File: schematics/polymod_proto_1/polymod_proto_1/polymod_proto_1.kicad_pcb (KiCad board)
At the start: 2 copper layers, 141 parts, among them J1 AudioJack2, J1 Conn_01x02_Male, J10 Conn_01x08_Male, J11 Conn_01x08_Male, J12 Conn_01x08_Male, J13 Conn_01x08_Male, J14 Conn_01x03_Male, J2 AudioJack3, J2 Conn_01x03_Male, J3 AudioJack2, J3 Conn_01x02_Male, J4 Barrel_Jack, J5 AudioJack3, J6 Conn_01x08_Male, J7 Conn_01x08_Male, J8 Conn_01x08_Male, J9 Conn_01x08_Male, SW1 SW_Push, SW2 SW_Push, SW3 SW_Push, SW4 SW_Push, SW5 SW_Push, SW6 SW_Push, SW7 SW_Push, SW8 SW_Push, U1 6N138, U10 74HC595, U11 74LS165, U12 74LS165, U13 74LS165, U2 74HC595, U3 74LS165, U4 4051, U5 74HC595, U6 74LS165, U7 4051, U8 74HC595, U9 74HC595

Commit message: layout going well
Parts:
- D10, D11, D12, D13, D14, D15, D16, D17, D18, D19, D20, D21, D22, D23, D24, D25, D26, D27, D28, D29, D30, D31, D32, D33, D34, D35, D36, D37, D38, D7, D8, D9: footprint Diode_THT:D_DO-35_SOD27_P7.62mm_Horizontal -> Diode_SMD:Nexperia_CFP3_SOD-123W
- moved C1 181.0 mm to (40.1, -81.9)
- moved D5 181.0 mm to (86.9, -120.7)
- moved D6 181.0 mm to (60.9, -92.2)
- moved J1 181.0 mm to (71.3, -105.7)
- moved JP1 181.0 mm to (75.9, -105.7)
- moved R1 181.0 mm to (55.0, -85.9)
- moved R10 181.0 mm to (94.2, -123.0)
- moved R5 181.0 mm to (98.6, -123.0)
- moved SW1 181.0 mm to (68.0, -122.5)
- moved SW5 181.0 mm to (49.9, -93.9)
- moved U2 181.0 mm to (53.3, -118.8)
- moved U3 181.0 mm to (61.7, -118.8)
- moved U4 181.0 mm to (160.1, -118.8)
- moved D1 181.0 mm to (47.7, -76.3)
- moved D2 181.0 mm to (47.8, -82.0)
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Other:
- board text added: "TEST LABEL TEST LABEL TEST LABEL TEST LABEL TEST LABEL TEST LABEL TEST LABEL TEST LABEL"

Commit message: components pretty much in place
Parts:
- removed the J1 at (71.3, -105.7)
- removed the J2 at (44.3, -93.2)
- removed the J3 at (71.3, -98.5)
- removed J5: AudioJack3, Connector_PinHeader_2.54mm:PinHeader_1x03_P2.54mm_Vertical
- SW1, SW2, SW3, SW4, SW5, SW6, SW7, SW8: footprint Button_Switch_THT:SW_PUSH_6mm_H4.3mm -> Button_Switch_THT:SW_PUSH-12mm
- moved SW6 335.5 mm to (215.9, 189.1), turned to 90 degrees
- moved SW7 333.5 mm to (188.0, 188.0), turned to 90 degrees
- moved SW8 331.9 mm to (200.7, 188.0), turned to 90 degrees
- moved J3 295.2 mm to (130.8, 132.1)
- moved J1 292.7 mm to (127.0, 132.1)
- moved SW5 282.8 mm to (198.1, 146.9), turned to 90 degrees
- moved SW1 278.3 mm to (137.2, 147.1), turned to 90 degrees
- moved SW2 277.3 mm to (152.4, 147.1), turned to 90 degrees
- moved SW3 271.5 mm to (167.7, 146.9), turned to 90 degrees
- moved SW4 270.3 mm to (182.9, 146.9), turned to 90 degrees
- moved D5 267.2 mm to (116.8, 144.8)
- moved R10 264.4 mm to (124.5, 139.7)
- moved D3 258.5 mm to (101.6, 144.8)
- moved U3 255.8 mm to (118.1, 130.8)
- moved U2 246.9 mm to (87.6, 125.7)
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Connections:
- J2 pad 2: /midi_in_ring -> /midi_out_ring
- J2 pad 3: /midi_in_tip -> /midi_out_tip
- R4 pad 2: /midi_in_ring -> /midi_out_ring
- R5 pad 1: /midi_in_tip -> /midi_out_tip

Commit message: routing started
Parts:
- removed SW6, SW7, SW8: SW_Push, Button_Switch_THT:SW_PUSH-12mm
- A1: moved to B.Cu
- moved U2 44.4 mm to (132.0, 124.0)
- moved U3 30.2 mm to (147.0, 122.0)
- moved J1 25.6 mm to (132.2, 107.0)
- moved J3 25.6 mm to (136.0, 107.0)
- moved A1 21.8 mm to (141.6, 62.5), turned to 180 degrees
- moved U4 20.8 mm to (148.0, 91.0)
- moved U7 20.2 mm to (148.0, 103.0)
- moved U10 8.71 mm to (88.0, 123.0), turned to 0 degrees
- moved U13 6.71 mm to (117.0, 126.0)
- moved R10 6.69 mm to (125.9, 146.2)
- moved R7 6.69 mm to (103.1, 146.2)
- moved R8 6.69 mm to (110.7, 146.2)
- moved R6 6.69 mm to (95.5, 146.2)
- moved R9 6.69 mm to (118.3, 146.2)
- moved R11 5.08 mm to (105.4, 55.9), turned to 180 degrees
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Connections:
- U3 pad 4: Net-(SW6-Pad2) -> unconnected-(U3-Pad4)
- U3 pad 5: Net-(SW7-Pad2) -> unconnected-(U3-Pad5)
- U3 pad 6: Net-(SW8-Pad2) -> unconnected-(U3-Pad6)
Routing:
- net Net-(SW5-Pad2): track 0.00 -> 77.5 mm
- net Net-(SW4-Pad2): track 0.00 -> 56.8 mm
- net Net-(R6-Pad1): track 0.00 -> 48.7 mm
- net Net-(R7-Pad1): track 0.00 -> 44.1 mm
- net Net-(SW3-Pad2): track 0.00 -> 41.5 mm
- net Net-(R8-Pad1): track 0.00 -> 39.3 mm
- net Net-(R9-Pad1): track 0.00 -> 32.7 mm
- net Net-(R10-Pad1): track 0.00 -> 30.4 mm
- net Net-(J7-Pad8): track 0.00 -> 29.5 mm
- net Net-(J12-Pad8): track 0.00 -> 29.4 mm
- net Net-(SW1-Pad2): track 0.00 -> 28.9 mm
- net Net-(J11-Pad8): track 0.00 -> 28.6 mm
- net Net-(J13-Pad8): track 0.00 -> 28.0 mm
- net Net-(SW2-Pad2): track 0.00 -> 28.0 mm
- net Net-(J7-Pad7): track 0.00 -> 27.8 mm
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- added copper zone on F.Cu, net GND

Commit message: routing is HARD
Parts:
- moved J14 63.5 mm to (172.5, 58.0), turned to 90 degrees
- moved D1 5.37 mm to (102.0, 38.0)
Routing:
- net VCC: track 0.00 -> 487.9 mm, vias 0 -> 4
- net PATCHING_OUT_LATCH: track 0.00 -> 124.9 mm, vias 0 -> 4
- net Net-(RV11-Pad2): track 0.00 -> 97.0 mm, vias 0 -> 2
- net /PATCHING_OUT_DATA: track 0.00 -> 83.8 mm, vias 0 -> 2
- net PATCHING_OUT_CLOCK: track 0.00 -> 74.8 mm, vias 0 -> 2
- net Net-(RV16-Pad2): track 0.00 -> 73.4 mm
- net Net-(RV12-Pad2): track 0.00 -> 65.7 mm
- net Net-(RV15-Pad2): track 0.00 -> 53.1 mm
- net Net-(RV14-Pad2): track 0.00 -> 47.6 mm, vias 0 -> 1
- net Net-(RV10-Pad2): track 0.00 -> 38.7 mm
- net 4051_ADDRESS_C: track 0.00 -> 34.7 mm
- net 4051_ADDRESS_B: track 0.00 -> 31.3 mm
- net 4051_ADDRESS_A: track 0.00 -> 26.1 mm
- net Net-(RV13-Pad2): track 0.00 -> 23.5 mm, vias 0 -> 1
- net Net-(RV9-Pad2): track 0.00 -> 17.9 mm
- added copper zone on B.Cu, net GND

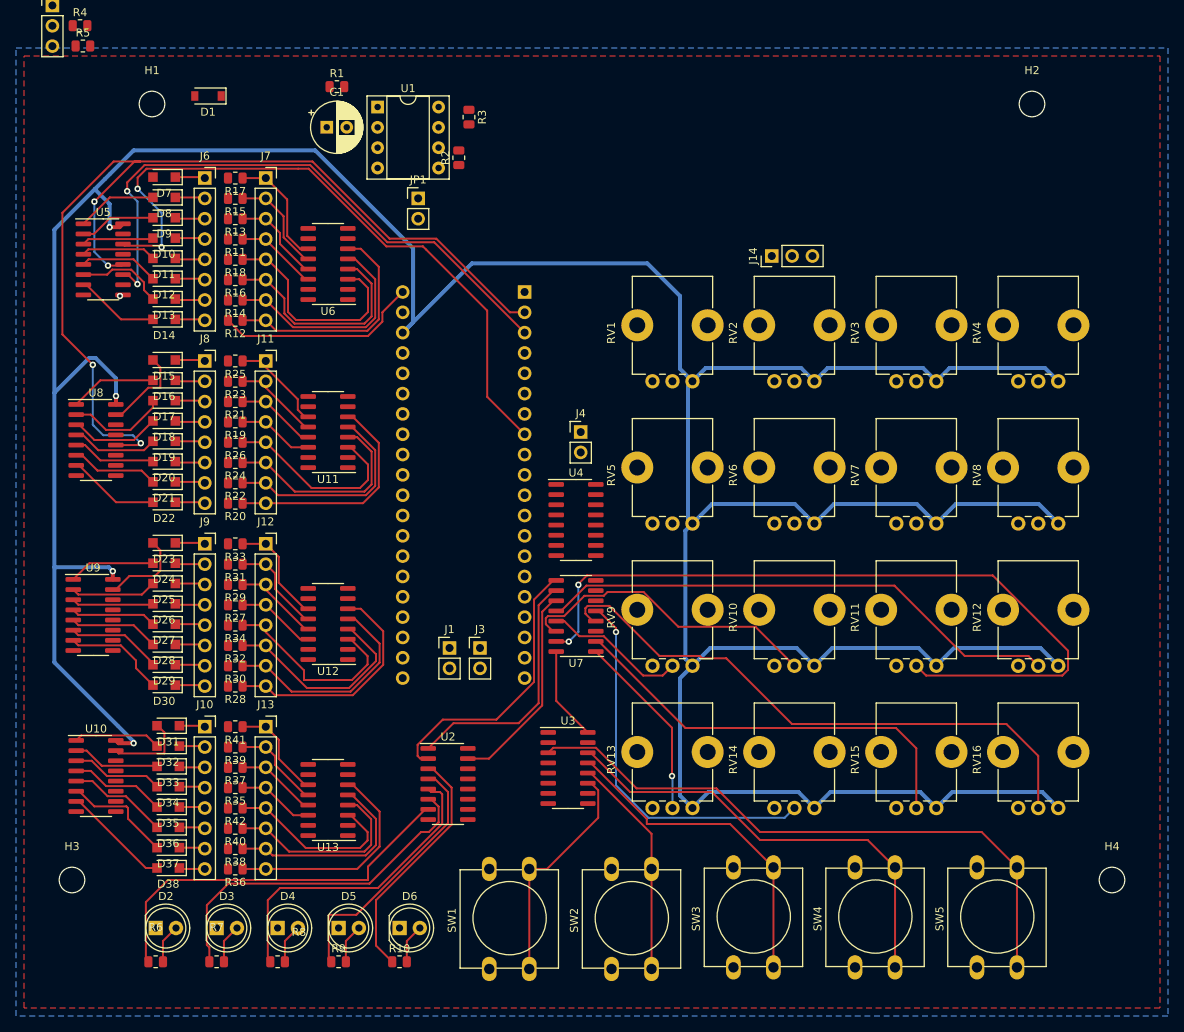
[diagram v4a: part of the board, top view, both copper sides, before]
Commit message: better layout/routing
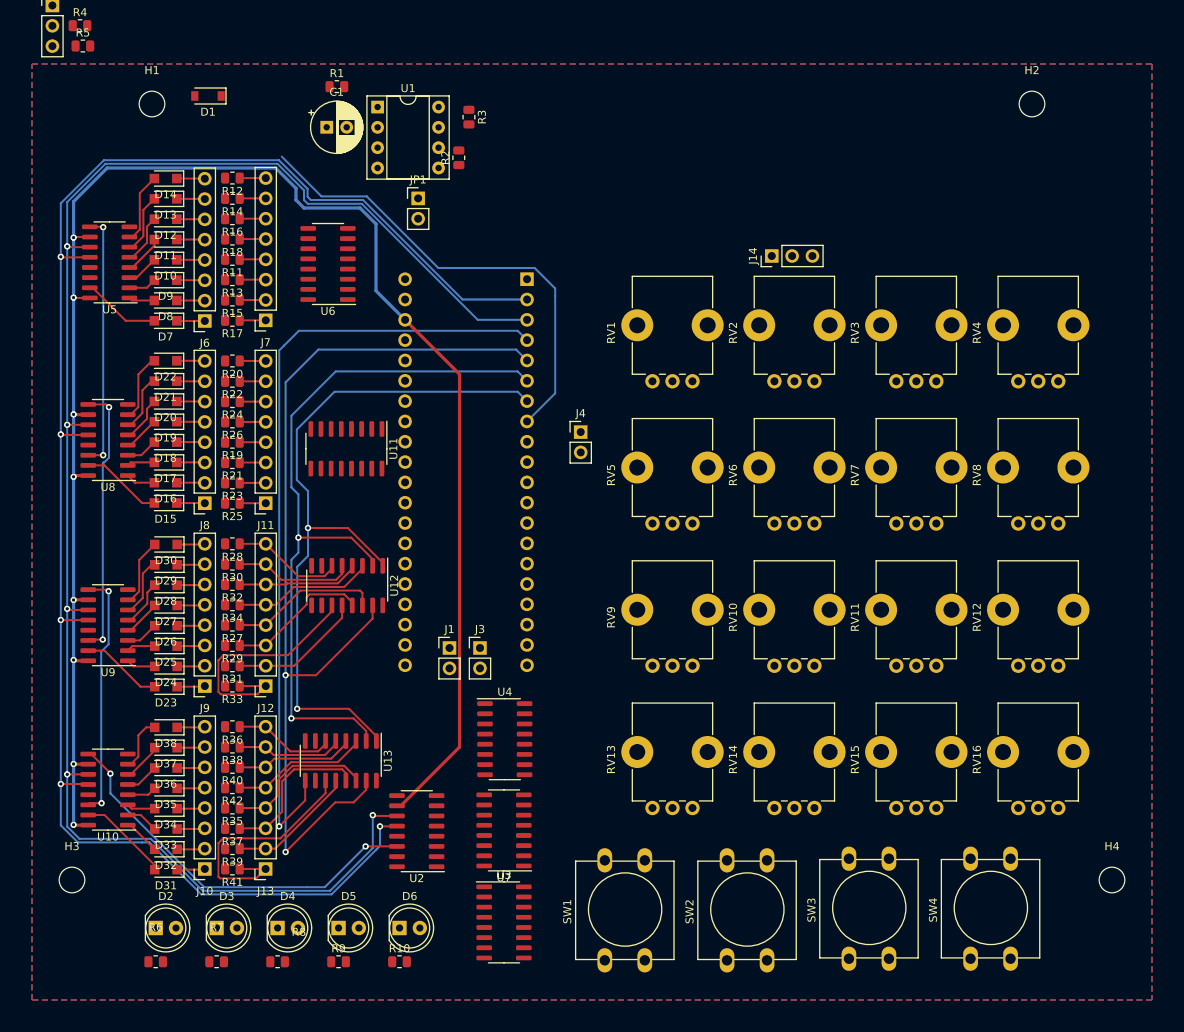
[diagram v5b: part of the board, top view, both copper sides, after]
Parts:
- removed SW5: SW_Push, Button_Switch_THT:SW_PUSH-12mm
- moved U4 28.8 mm to (139.1, 118.4)
- moved U7 28.3 mm to (139.0, 129.8)
- moved U3 20.9 mm to (139.0, 141.3)
- moved D31 18.0 mm to (96.7, 134.7)
- moved D23 18.0 mm to (96.7, 111.8)
- moved D7 18.0 mm to (96.7, 66.1)
- moved D15 17.9 mm to (96.7, 88.9)
- moved J6 17.9 mm to (101.6, 66.1), turned to 180 degrees
- moved R12 17.8 mm to (105.1, 48.3)
- moved R17 17.8 mm to (105.1, 66.0)
- moved R20 17.8 mm to (105.1, 71.1)
- moved R25 17.8 mm to (105.1, 88.9)
- moved R28 17.8 mm to (105.1, 94.0)
- moved R33 17.8 mm to (105.1, 111.8)
- moved R36 17.8 mm to (105.1, 116.8)
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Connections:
- U3 pad 3: Net-(SW5-Pad2) -> unconnected-(U3-Pad3)
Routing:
- net VCC: track 487.9 -> 217.0 mm, vias 4 -> 8
- net PATCHING_OUT_CLOCK: track 74.8 -> 208.0 mm, vias 2 -> 5
- net PATCHING_IN_CE: track 0.00 -> 121.0 mm, vias 0 -> 2
- net /PATCHING_IN_DATA: track 0.00 -> 99.1 mm, vias 0 -> 1
- net Net-(RV11-Pad2): track 97.0 -> 0.00 mm, vias 2 -> 0
- net PATCHING_IN_CLOCK: track 0.00 -> 93.3 mm, vias 0 -> 2
- net PATCHING_IN_LOAD: track 0.00 -> 90.8 mm, vias 0 -> 2
- net PATCHING_OUT_LATCH: track 124.9 -> 210.6 mm, vias 4 -> 5
- net Net-(SW5-Pad2): track 77.5 -> 0.00 mm
- net Net-(RV16-Pad2): track 73.4 -> 0.00 mm
- net Net-(RV12-Pad2): track 65.7 -> 0.00 mm
- net Net-(SW4-Pad2): track 56.8 -> 0.00 mm
- net Net-(RV15-Pad2): track 53.1 -> 0.00 mm
- net /UTIL_595: track 0.00 -> 49.1 mm, vias 0 -> 2
- net Net-(R6-Pad1): track 48.7 -> 0.00 mm
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
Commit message: ummm less sure this is working well but not awful
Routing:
- net VCC: track 217.0 -> 507.5 mm
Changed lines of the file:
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@@
   )
   (segment (start 125.625 126.725) (end 126.107138 126.725) (width 0.4) (layer "F.Cu") (net 3))
+  (segment (start 206.980489 107.920489) (end 208.28 109.22) (width 0.4) (layer "F.Cu") (net 3))
+  (segment (start 191.740489 107.920489) (end 193.04 109.22) (width 0.4) (layer "F.Cu") (net 3))
+  (segment (start 162.56 109.22) (end 163.859511 107.920489) (width 0.4) (layer "F.Cu") (net 3))
   (segment (start 87.225 55.625) (end 85.275 55.625) (width 0.25) (layer "F.Cu") (net 3))
+  (segment (start 206.980489 72.360489) (end 208.28 73.66) (width 0.4) (layer "F.Cu") (net 3))
+  (segment (start 177.8 73.66) (end 179.099511 72.360489) (width 0.4) (layer "F.Cu") (net 3))
+  (segment (start 161.66 110.12) (end 161.66 126.1) (width 0.4) (layer "F.Cu") (net 3))
+  (segment (start 163.859511 107.920489) (end 176.500489 107.920489) (width 0.4) (layer "F.Cu") (net 3))
+  (segment (start 176.500489 107.920489) (end 177.8 109.22) (width 0.4) (layer "F.Cu") (net 3))
   (segment (start 87.025 77.825) (end 85.225 77.825) (width 0.4) (layer "F.Cu") (net 3))
+  (segment (start 191.740489 72.360489) (end 193.04 73.66) (width 0.4) (layer "F.Cu") (net 3))
+  (segment (start 206.980489 125.700489) (end 208.28 127) (width 0.4) (layer "F.Cu") (net 3))
+  (segment (start 161.66 74.56) (end 161.66 90.54) (width 0.4) (layer "F.Cu") (net 3))
+  (segment (start 162.56 109.22) (end 161.66 110.12) (width 0.4) (layer "F.Cu") (net 3))
   (segment (start 85.245 63.245) (end 85.2 63.2) (width 0.25) (layer "F.Cu") (net 3))
   (segment (start 87.025 100.975) (end 85.225 100.975) (width 0.4) (layer "F.Cu") (net 3))
   (segment (start 87.025 108.595) (end 85.295 108.595) (width 0.4) (layer "F.Cu") (net 3))
+  (segment (start 194.339511 72.360489) (end 206.980489 72.360489) (width 0.4) (layer "F.Cu") (net 3))
+  (segment (start 161.66 126.1) (end 162.56 127) (width 0.4) (layer "F.Cu") (net 3))
   (segment (start 85.355 85.445) (end 85.2 85.6) (width 0.4) (layer "F.Cu") (net 3))
+  (segment (start 162.56 127) (end 163.859511 125.700489) (width 0.4) (layer "F.Cu") (net 3))
+  (segment (start 194.339511 107.920489) (end 206.980489 107.920489) (width 0.4) (layer "F.Cu") (net 3))
+  (segment (start 179.099511 107.920489) (end 191.740489 107.920489) (width 0.4) (layer "F.Cu") (net 3))
   (segment (start 86.98 129.1) (end 87.025 129.145) (width 0.4) (layer "F.Cu") (net 3))
   (segment (start 85.225 100.975) (end 85.2 101) (width 0.4) (layer "F.Cu") (net 3))
+  (segment (start 162.56 91.44) (end 163.859511 90.140489) (width 0.4) (layer "F.Cu") (net 3))
+  (segment (start 162.56 73.66) (end 163.859511 72.360489) (width 0.4) (layer "F.Cu") (net 3))
+  (segment (start 179.099511 72.360489) (end 191.740489 72.360489) (width 0.4) (layer "F.Cu") (net 3))
+  (segment (start 177.8 109.22) (end 179.099511 107.920489) (width 0.4) (layer "F.Cu") (net 3))
+  (segment (start 176.500489 72.360489) (end 177.8 73.66) (width 0.4) (layer "F.Cu") (net 3))
+  (segment (start 163.859511 90.140489) (end 176.500489 90.140489) (width 0.4) (layer "F.Cu") (net 3))
+  (segment (start 193.04 127) (end 194.339511 125.700489) (width 0.4) (layer "F.Cu") (net 3))
   (segment (start 85.275 55.625) (end 85.2 55.7) (width 0.25) (layer "F.Cu") (net 3))
+  (segment (start 206.980489 90.140489) (end 208.28 91.44) (width 0.4) (layer "F.Cu") (net 3))
   (segment (start 87.025 129.145) (end 85.245 129.145) (width 0.4) (layer "F.Cu") (net 3))
   (segment (start 133.439511 72.782011) (end 126.6375 65.98) (width 0.4) (layer "F.Cu") (net 3))
+  (segment (start 191.740489 125.700489) (end 193.04 127) (width 0.4) (layer "F.Cu") (net 3))
+  (segment (start 177.8 127) (end 179.099511 125.700489) (width 0.4) (layer "F.Cu") (net 3))
   (segment (start 87.025 85.445) (end 85.355 85.445) (width 0.4) (layer "F.Cu") (net 3))
+  (segment (start 191.740489 90.140489) (end 193.04 91.44) (width 0.4) (layer "F.Cu") (net 3))
+  (segment (start 193.04 109.22) (end 194.339511 107.920489) (width 0.4) (layer "F.Cu") (net 3))
   (segment (start 85.225 77.825) (end 85.2 77.8) (width 0.4) (layer "F.Cu") (net 3))
+  (segment (start 176.500489 125.700489) (end 177.8 127) (width 0.4) (layer "F.Cu") (net 3))
   (segment (start 85.225 121.525) (end 85.2 121.5) (width 0.4) (layer "F.Cu") (net 3))
+  (segment (start 130.4575 69.8) (end 158.7 69.8) (width 0.4) (layer "F.Cu") (net 3))
+  (segment (start 162.56 91.44) (end 161.66 92.34) (width 0.4) (layer "F.Cu") (net 3))
+  (segment (start 193.04 91.44) (end 194.339511 90.140489) (width 0.4) (layer "F.Cu") (net 3))
   (segment (start 85.245 129.145) (end 85.2 129.1) (width 0.4) (layer "F.Cu") (net 3))
+  (segment (start 161.66 92.34) (end 161.66 108.32) (width 0.4) (layer "F.Cu") (net 3))
+  (segment (start 163.859511 125.700489) (end 176.500489 125.700489) (width 0.4) (layer "F.Cu") (net 3))
+  (segment (start 158.7 69.8) (end 162.56 73.66) (width 0.4) (layer "F.Cu") (net 3))
   (segment (start 85.295 108.595) (end 85.2 108.5) (width 0.4) (layer "F.Cu") (net 3))
   (segment (start 87.225 63.245) (end 85.245 63.245) (width 0.25) (layer "F.Cu") (net 3))
+  (segment (start 179.099511 90.140489) (end 191.740489 90.140489) (width 0.4) (layer "F.Cu") (net 3))
+  (segment (start 177.8 91.44) (end 179.099511 90.140489) (width 0.4) (layer "F.Cu") (net 3))
+  (segment (start 179.099511 125.700489) (end 191.740489 125.700489) (width 0.4) (layer "F.Cu") (net 3))
+  (segment (start 126.6375 65.98) (end 130.4575 69.8) (width 0.4) (layer "F.Cu") (net 3))
   (segment (start 126.107138 126.725) (end 133.439511 119.392627) (width 0.4) (layer "F.Cu") (net 3))
+  (segment (start 176.500489 90.140489) (end 177.8 91.44) (width 0.4) (layer "F.Cu") (net 3))
   (segment (start 133.439511 119.392627) (end 133.439511 72.782011) (width 0.4) (layer "F.Cu") (net 3))
+  (segment (start 162.56 73.66) (end 161.66 74.56) (width 0.4) (layer "F.Cu") (net 3))
+  (segment (start 194.339511 90.140489) (end 206.980489 90.140489) (width 0.4) (layer "F.Cu") (net 3))
   (segment (start 87.025 121.525) (end 85.225 121.525) (width 0.4) (layer "F.Cu") (net 3))
+  (segment (start 194.339511 125.700489) (end 206.980489 125.700489) (width 0.4) (layer "F.Cu") (net 3))
+  (segment (start 161.66 90.54) (end 162.56 91.44) (width 0.4) (layer "F.Cu") (net 3))
+  (segment (start 163.859511 72.360489) (end 176.500489 72.360489) (width 0.4) (layer "F.Cu") (net 3))
+  (segment (start 161.66 108.32) (end 162.56 109.22) (width 0.4) (layer "F.Cu") (net 3))
+  (segment (start 193.04 73.66) (end 194.339511 72.360489) (width 0.4) (layer "F.Cu") (net 3))
   (via (at 85.2 63.2) (size 0.8) (drill 0.4) (layers "F.Cu" "B.Cu") (net 3))
   (via (at 85.2 77.8) (size 0.8) (drill 0.4) (layers "F.Cu" "B.Cu") (net 3))

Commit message: about to restart routing again
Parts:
- moved U1 80.5 mm to (203.2, 48.2)
- moved C1 25.5 mm to (108.0, 18.0)
- moved R3 24.0 mm to (130.0, 17.1)
- moved R2 22.0 mm to (130.0, 24.0)
- moved R1 12.6 mm to (113.9, 25.0)
- moved J14 12.5 mm to (184.9, 56.5)
- moved D1 11.4 mm to (105.0, 27.0)
- moved U11 8.80 mm to (118.0, 73.4), turned to 0 degrees
- moved U6 4.00 mm to (117.0, 55.0)
- moved RV1 3.99 mm to (166.5, 73.0)
- moved RV10 3.99 mm to (181.7, 108.6)
- moved RV11 3.99 mm to (197.0, 108.6)
- moved RV12 3.99 mm to (212.2, 108.6)
- moved RV13 3.99 mm to (166.5, 126.4)
- moved RV14 3.99 mm to (181.7, 126.4)
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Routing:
- net VCC: track 507.5 -> 479.3 mm
- net Net-(J11-Pad1): track 3.25 -> 28.5 mm
- net Net-(J11-Pad3): track 3.25 -> 21.4 mm
- net Net-(J11-Pad2): track 3.25 -> 21.4 mm
- net Net-(J11-Pad4): track 3.25 -> 21.3 mm
- net Net-(J11-Pad5): track 3.25 -> 19.3 mm
- net Net-(J11-Pad6): track 3.25 -> 16.7 mm
- net Net-(J11-Pad7): track 3.25 -> 14.5 mm
- net Net-(J11-Pad8): track 3.25 -> 11.3 mm
